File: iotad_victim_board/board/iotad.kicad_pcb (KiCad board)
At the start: 2 copper layers, 24.8 x 29 mm, 5 parts, among them P1 CONN_01X09, P2 CONN_01X06, U1 24C16, U2 MAX31820

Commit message: today
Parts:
- removed the P1 at (125.9, 124.6)
- removed the P2 at (143.9, 111.0)
- removed the R1 at (131.4, 124.7)
- removed the U1 at (134.4, 112.6)
- removed the U2 at (141.3, 123.8)
- added P1: CONN_01X09, Pin_Headers:Pin_Header_Straight_1x09, F.Cu at (153.4, 124.2)
- added P1: CONN_01X09, Pin_Headers:Pin_Header_Straight_1x09, F.Cu at (139.4, 124.2)
- added P2: CONN_01X06, Pin_Headers:Pin_Header_Straight_1x06, F.Cu at (163.1, 103.9)
- added P2: CONN_01X06, Pin_Headers:Pin_Header_Straight_1x06, F.Cu at (149.1, 103.9)
- added R1: 4.8k, Resistors_SMD:R_1206_HandSoldering, F.Cu at (158.2, 115.6)
- added R1: 4.8k, Resistors_SMD:R_1206_HandSoldering, F.Cu at (144.3, 115.6)
- added REF**11111: via, via, F.Cu at (152.7, 127.5)
- added REF**11111: via, via, F.Cu at (160.3, 126.2)
- added REF**11111: via, via, F.Cu at (160.5, 119.1)
- added REF**11111: via, via, F.Cu at (156.7, 106.4)
- added REF**11111: via, via, F.Cu at (146.3, 126.2)
- added REF**11111: via, via, F.Cu at (138.7, 127.5)
- added REF**11111: via, via, F.Cu at (146.6, 119.1)
- added REF**11111: via, via, F.Cu at (142.7, 106.4)
- added REF**11121: via, via, F.Cu at (161.8, 126.2)
- added REF**11121: via, via, F.Cu at (154.2, 127.5)
- added REF**11121: via, via, F.Cu at (162.0, 119.1)
- added REF**11121: via, via, F.Cu at (158.2, 106.4)
- added REF**11121: via, via, F.Cu at (147.8, 126.2)
- added REF**11121: via, via, F.Cu at (140.2, 127.5)
- added REF**11121: via, via, F.Cu at (148.1, 119.1)
- added REF**11121: via, via, F.Cu at (144.2, 106.4)
- added REF**11131: via, via, F.Cu at (155.7, 127.5)
- added REF**11131: via, via, F.Cu at (163.5, 119.1)
- added REF**11131: via, via, F.Cu at (163.3, 126.2)
- added REF**11131: via, via, F.Cu at (159.7, 106.4)
- added REF**11131: via, via, F.Cu at (149.3, 126.2)
- added REF**11131: via, via, F.Cu at (141.7, 127.5)
- added REF**11131: via, via, F.Cu at (149.6, 119.1)
- added REF**11131: via, via, F.Cu at (145.7, 106.4)
- added U1: 24C16, SMD_Packages:SOIC-8-N, F.Cu at (158.5, 106.2)
- added U1: 24C16, SMD_Packages:SOIC-8-N, F.Cu at (144.5, 106.2)
- added U2: MAX31820, TO_SOT_Packages_THT:TO-92_Molded_Wide, F.Cu at (163.6, 121.9)
- added U2: MAX31820, TO_SOT_Packages_THT:TO-92_Molded_Wide, F.Cu at (149.6, 121.9)
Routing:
- net VCC: track 45.2 -> 61.2 mm
- net DATA: track 13.7 -> 29.5 mm
- net TX: track 18.3 -> 28.3 mm
- net RX: track 18.3 -> 26.5 mm
- net SCL: track 5.30 -> 11.6 mm
- net SDA: track 5.82 -> 6.67 mm
- added copper zone on B.Cu, net Net-(P1-Pad8)
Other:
- board size 24.8 x 29 mm -> 27.9 x 27.9 mm
- board text added: "3.3v"
- board text added: "D1W"
- board text added: "GND"
- board text added: "IoTAD Victim Board v1.01"
- board text added: "RX"
- board text added: "SCL"
- board text added: "SDA"
- board text added: "TX"
- board text added: "dsgn: jegeva 2016"

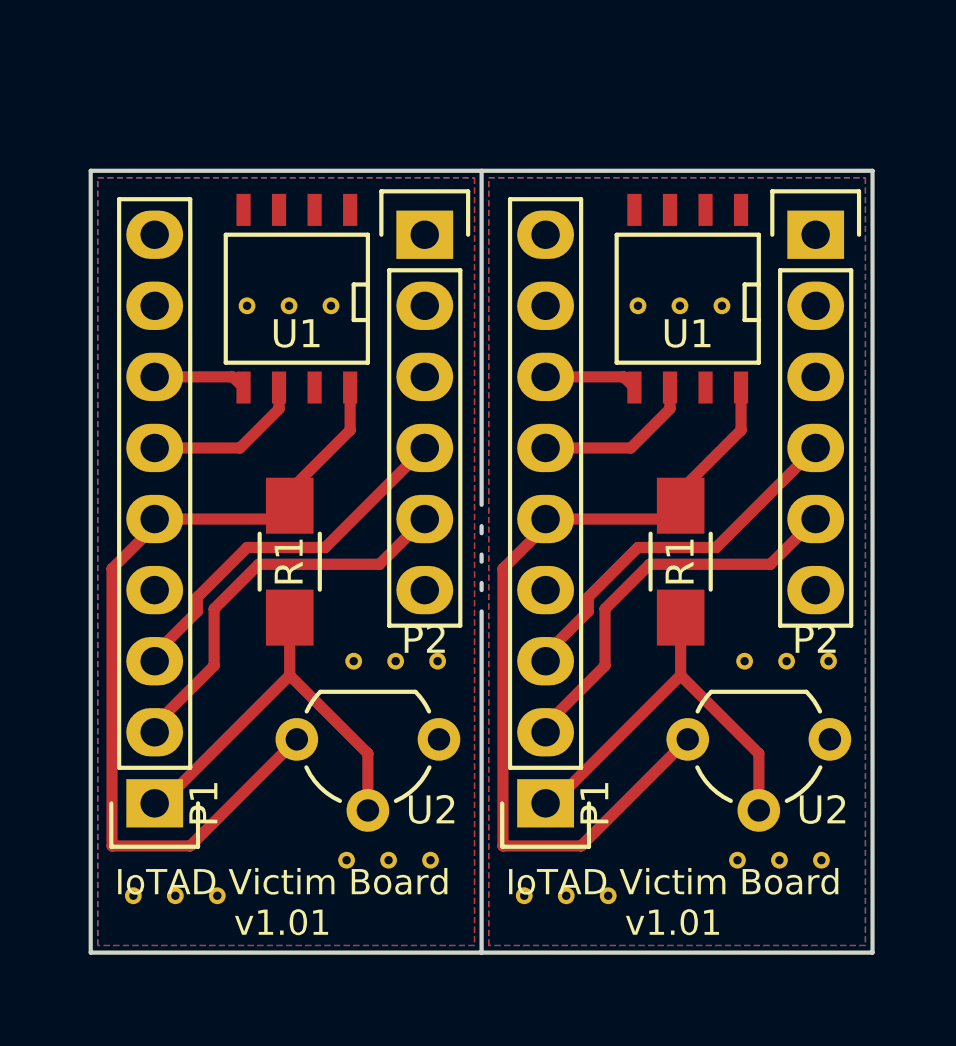
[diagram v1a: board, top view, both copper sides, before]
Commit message: harcoded password
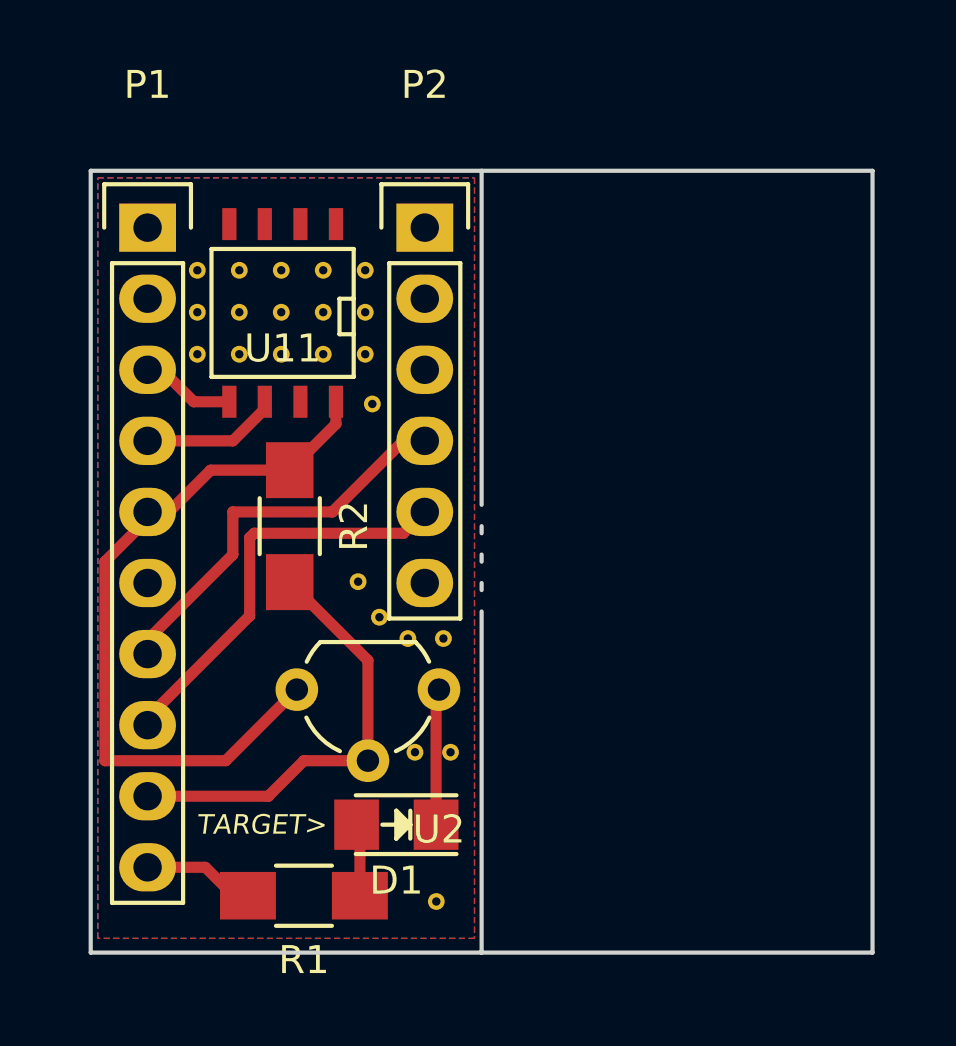
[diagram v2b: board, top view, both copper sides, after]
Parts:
- removed the P1 at (153.4, 124.2)
- removed the P1 at (139.4, 124.2)
- removed the P2 at (163.1, 103.9)
- removed the P2 at (149.1, 103.9)
- removed the R1 at (158.2, 115.6)
- removed the R1 at (144.3, 115.6)
- removed REF**11111 (x8), REF**11121 (x8), REF**11131 (x8): via, via
- removed U1 (x2): 24C16, SMD_Packages:SOIC-8-N
- removed the U2 at (163.6, 121.9)
- removed the U2 at (149.6, 121.9)
- added D1: LED, LEDs:LED_1206, F.Cu at (148.1, 125.0)
- added P1: CONN_01X10, Pin_Headers:Pin_Header_Straight_1x10, F.Cu at (139.2, 103.6)
- added P2: CONN_01X06, Pin_Headers:Pin_Header_Straight_1x06, F.Cu at (149.1, 103.6)
- added R1: R, Resistors_SMD:R_1206_HandSoldering, F.Cu at (144.8, 127.5)
- added R2: 4.8k, Resistors_SMD:R_1206_HandSoldering, F.Cu at (144.3, 114.3)
- added REF**1111: VIA-0.6mm, via-0:VIA-0.6mm, F.Cu at (141.0, 105.2)
- added REF**1112: VIA-0.6mm, via-0:VIA-0.6mm, F.Cu at (141.0, 106.7)
- added REF**1113: VIA-0.6mm, via-0:VIA-0.6mm, F.Cu at (141.0, 108.2)
- added REF**1121: VIA-0.6mm, via-0:VIA-0.6mm, F.Cu at (142.5, 105.2)
- added REF**1122: VIA-0.6mm, via-0:VIA-0.6mm, F.Cu at (142.5, 106.7)
- added REF**1123: VIA-0.6mm, via-0:VIA-0.6mm, F.Cu at (142.5, 108.2)
- added REF**1131: VIA-0.6mm, via-0:VIA-0.6mm, F.Cu at (144.0, 105.2)
- added REF**1132: VIA-0.6mm, via-0:VIA-0.6mm, F.Cu at (144.0, 106.7)
- added REF**1133: VIA-0.6mm, via-0:VIA-0.6mm, F.Cu at (144.0, 108.2)
- added REF**1141: VIA-0.6mm, via-0:VIA-0.6mm, F.Cu at (145.5, 105.2)
- added REF**1142: VIA-0.6mm, via-0:VIA-0.6mm, F.Cu at (145.5, 106.7)
- added REF**1143: VIA-0.6mm, via-0:VIA-0.6mm, F.Cu at (145.5, 108.2)
- added REF**1151: VIA-0.6mm, via-0:VIA-0.6mm, F.Cu at (147.0, 105.2)
- added REF**1152: VIA-0.6mm, via-0:VIA-0.6mm, F.Cu at (147.0, 106.7)
- added REF**1153: VIA-0.6mm, via-0:VIA-0.6mm, F.Cu at (149.5, 127.7)
- added REF**1153: VIA-0.6mm, via-0:VIA-0.6mm, F.Cu at (148.7, 122.4)
- added REF**1153: VIA-0.6mm, via-0:VIA-0.6mm, F.Cu at (150.0, 122.4)
- added REF**1153: VIA-0.6mm, via-0:VIA-0.6mm, F.Cu at (148.5, 118.3)
- added REF**1153: VIA-0.6mm, via-0:VIA-0.6mm, F.Cu at (149.8, 118.3)
- added REF**1153: VIA-0.6mm, via-0:VIA-0.6mm, F.Cu at (147.5, 117.6)
- added REF**1153: VIA-0.6mm, via-0:VIA-0.6mm, F.Cu at (146.7, 116.3)
- added REF**1153: VIA-0.6mm, via-0:VIA-0.6mm, F.Cu at (147.2, 109.9)
- added REF**1153: VIA-0.6mm, via-0:VIA-0.6mm, F.Cu at (147.0, 108.2)
- added U11: 24C16, SMD_Packages:SOIC-8-N, F.Cu at (144.0, 106.7)
- added U2: MAX31820, TO_SOT_Packages_THT:TO-92_Molded_Wide, F.Cu at (149.6, 120.1)
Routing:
- net VCC: track 61.2 -> 26.3 mm
- net DATA: track 29.5 -> 15.9 mm
- net TX: track 28.3 -> 14.8 mm
- net RX: track 26.5 -> 14.3 mm
- net SCL: track 11.6 -> 4.92 mm
- net GND: track 0.00 -> 4.87 mm
- net Net-(P1-Pad10): track 0.00 -> 4.22 mm
- net SDA: track 6.67 -> 3.39 mm
- net Net-(D1-Pad2): track 0.00 -> 2.59 mm
- added copper zone on B.Cu, net GND
- added copper zone on F.Cu, net GND
- removed copper zone on B.Cu, net Net-(P1-Pad8)
- removed copper zone on F.Cu, net Net-(P1-Pad8)
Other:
- board text added: "IoTAD v1.2 24/02/2016 JGV"
- board text added: "Rx"
- board text added: "TARGET>"
- board text added: "Tx"
- board text added: "T° Data"
- board text added: "VCC"
- board text removed: "3.3v"
- board text removed: "D1W"
- board text removed: "IoTAD Victim Board v1.01"
- board text removed: "RX"
- board text removed: "TX"
- board text removed: "dsgn: jegeva 2016"

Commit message: storing
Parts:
- added D1: LED, LEDs:LED_1206, F.Cu at (182.6, 127.5)
- added D1: LED, LEDs:LED_1206, F.Cu at (197.4, 127.5)
- added D1: LED, LEDs:LED_1206, F.Cu at (227.1, 127.5)
- added D1: LED, LEDs:LED_1206, F.Cu at (212.3, 127.5)
- added D1: LED, LEDs:LED_1206, F.Cu at (153.2, 127.5)
- added D1: LED, LEDs:LED_1206, F.Cu at (167.9, 127.5)
- added D1: LED, LEDs:LED_1206, F.Cu at (138.2, 127.5)
- added P1: CONN_01X10, Pin_Headers:Pin_Header_Straight_1x10, F.Cu at (173.7, 106.2)
- added P1: CONN_01X10, Pin_Headers:Pin_Header_Straight_1x10, F.Cu at (188.5, 106.2)
- added P1: CONN_01X10, Pin_Headers:Pin_Header_Straight_1x10, F.Cu at (218.2, 106.2)
- added P1: CONN_01X10, Pin_Headers:Pin_Header_Straight_1x10, F.Cu at (203.5, 106.2)
- added P1: CONN_01X10, Pin_Headers:Pin_Header_Straight_1x10, F.Cu at (144.3, 106.2)
- added P1: CONN_01X10, Pin_Headers:Pin_Header_Straight_1x10, F.Cu at (159.0, 106.2)
- added P1: CONN_01X10, Pin_Headers:Pin_Header_Straight_1x10, F.Cu at (129.3, 106.2)
- added P2: CONN_01X06, Pin_Headers:Pin_Header_Straight_1x06, F.Cu at (183.6, 118.4)
- added P2: CONN_01X06, Pin_Headers:Pin_Header_Straight_1x06, F.Cu at (198.4, 118.4)
- added P2: CONN_01X06, Pin_Headers:Pin_Header_Straight_1x06, F.Cu at (228.1, 118.4)
- added P2: CONN_01X06, Pin_Headers:Pin_Header_Straight_1x06, F.Cu at (213.4, 118.4)
- added P2: CONN_01X06, Pin_Headers:Pin_Header_Straight_1x06, F.Cu at (154.2, 118.4)
- added P2: CONN_01X06, Pin_Headers:Pin_Header_Straight_1x06, F.Cu at (168.9, 118.4)
- added P2: CONN_01X06, Pin_Headers:Pin_Header_Straight_1x06, F.Cu at (139.2, 118.4)
- added R1: R, Resistors_SMD:R_1206_HandSoldering, F.Cu at (179.3, 130.0)
- added R1: R, Resistors_SMD:R_1206_HandSoldering, F.Cu at (194.1, 130.0)
- added R1: R, Resistors_SMD:R_1206_HandSoldering, F.Cu at (223.8, 130.0)
- added R1: R, Resistors_SMD:R_1206_HandSoldering, F.Cu at (209.0, 130.0)
- added R1: R, Resistors_SMD:R_1206_HandSoldering, F.Cu at (149.9, 130.0)
- added R1: R, Resistors_SMD:R_1206_HandSoldering, F.Cu at (164.6, 130.0)
- added R1: R, Resistors_SMD:R_1206_HandSoldering, F.Cu at (134.9, 130.0)
- added R2: 4.8k, Resistors_SMD:R_1206_HandSoldering, F.Cu at (178.8, 116.8)
- added R2: 4.8k, Resistors_SMD:R_1206_HandSoldering, F.Cu at (193.5, 116.8)
- added R2: 4.8k, Resistors_SMD:R_1206_HandSoldering, F.Cu at (223.3, 116.8)
- added R2: 4.8k, Resistors_SMD:R_1206_HandSoldering, F.Cu at (208.5, 116.8)
- added R2: 4.8k, Resistors_SMD:R_1206_HandSoldering, F.Cu at (149.4, 116.8)
- added R2: 4.8k, Resistors_SMD:R_1206_HandSoldering, F.Cu at (164.1, 116.8)
- added R2: 4.8k, Resistors_SMD:R_1206_HandSoldering, F.Cu at (134.4, 116.8)
- added REF** (x4): DRILL-0.6mm, via-0:DRILL-0.6mm, F.Cu at (186.2, 107.7)
- added REF** (x4): DRILL-0.6mm, via-0:DRILL-0.6mm, F.Cu at (186.2, 104.6)
- added REF** (x4): DRILL-0.6mm, via-0:DRILL-0.6mm, F.Cu at (186.2, 121.9)
- added REF** (x4): DRILL-0.6mm, via-0:DRILL-0.6mm, F.Cu at (186.2, 124.0)
- added REF** (x4): DRILL-0.6mm, via-0:DRILL-0.6mm, F.Cu at (186.2, 122.9)
- added REF** (x4): DRILL-0.6mm, via-0:DRILL-0.6mm, F.Cu at (215.9, 124.0)
- added REF** (x4): DRILL-0.6mm, via-0:DRILL-0.6mm, F.Cu at (215.9, 122.9)
- added REF** (x4): DRILL-0.6mm, via-0:DRILL-0.6mm, F.Cu at (215.9, 121.9)
- added REF** (x4): DRILL-0.6mm, via-0:DRILL-0.6mm, F.Cu at (215.9, 120.9)
- added REF** (x4): DRILL-0.6mm, via-0:DRILL-0.6mm, F.Cu at (186.2, 105.7)
- added REF** (x4): DRILL-0.6mm, via-0:DRILL-0.6mm, F.Cu at (215.9, 126.0)
- added REF** (x4): DRILL-0.6mm, via-0:DRILL-0.6mm, F.Cu at (215.9, 125.0)
- added REF** (x4): DRILL-0.6mm, via-0:DRILL-0.6mm, F.Cu at (215.9, 128.0)
- added REF** (x4): DRILL-0.6mm, via-0:DRILL-0.6mm, F.Cu at (215.9, 127.0)
- added REF** (x4): DRILL-0.6mm, via-0:DRILL-0.6mm, F.Cu at (215.9, 130.0)
- added REF** (x4): DRILL-0.6mm, via-0:DRILL-0.6mm, F.Cu at (215.9, 129.0)
- added REF** (x4): DRILL-0.6mm, via-0:DRILL-0.6mm, F.Cu at (215.9, 131.1)
- added REF** (x4): DRILL-0.6mm, via-0:DRILL-0.6mm, F.Cu at (215.9, 115.8)
- added REF** (x4): DRILL-0.6mm, via-0:DRILL-0.6mm, F.Cu at (215.9, 114.8)
- added REF** (x4): DRILL-0.6mm, via-0:DRILL-0.6mm, F.Cu at (215.9, 113.8)
- added REF** (x4): DRILL-0.6mm, via-0:DRILL-0.6mm, F.Cu at (215.9, 112.8)
- added REF** (x4): DRILL-0.6mm, via-0:DRILL-0.6mm, F.Cu at (215.9, 117.9)
- added REF** (x4): DRILL-0.6mm, via-0:DRILL-0.6mm, F.Cu at (186.2, 109.7)
- added REF** (x4): DRILL-0.6mm, via-0:DRILL-0.6mm, F.Cu at (215.9, 116.8)
- added REF** (x4): DRILL-0.6mm, via-0:DRILL-0.6mm, F.Cu at (215.9, 119.9)
- added REF** (x4): DRILL-0.6mm, via-0:DRILL-0.6mm, F.Cu at (215.9, 118.9)
- added REF** (x4): DRILL-0.6mm, via-0:DRILL-0.6mm, F.Cu at (186.2, 108.7)
- added REF** (x4): DRILL-0.6mm, via-0:DRILL-0.6mm, F.Cu at (215.9, 111.8)
- added REF** (x4): DRILL-0.6mm, via-0:DRILL-0.6mm, F.Cu at (215.9, 110.7)
- added REF** (x4): DRILL-0.6mm, via-0:DRILL-0.6mm, F.Cu at (215.9, 109.7)
- added REF** (x4): DRILL-0.6mm, via-0:DRILL-0.6mm, F.Cu at (215.9, 108.7)
- added REF** (x4): DRILL-0.6mm, via-0:DRILL-0.6mm, F.Cu at (186.2, 106.7)
- added REF** (x4): DRILL-0.6mm, via-0:DRILL-0.6mm, F.Cu at (215.9, 105.7)
- added REF** (x4): DRILL-0.6mm, via-0:DRILL-0.6mm, F.Cu at (215.9, 104.6)
- added REF** (x4): DRILL-0.6mm, via-0:DRILL-0.6mm, F.Cu at (215.9, 107.7)
- added REF** (x4): DRILL-0.6mm, via-0:DRILL-0.6mm, F.Cu at (215.9, 106.7)
- added REF** (x4): DRILL-0.6mm, via-0:DRILL-0.6mm, F.Cu at (200.9, 124.2)
- added REF** (x4): DRILL-0.6mm, via-0:DRILL-0.6mm, F.Cu at (200.9, 123.2)
- added REF** (x4): DRILL-0.6mm, via-0:DRILL-0.6mm, F.Cu at (200.9, 122.2)
- added REF** (x4): DRILL-0.6mm, via-0:DRILL-0.6mm, F.Cu at (200.9, 121.2)
- added REF** (x4): DRILL-0.6mm, via-0:DRILL-0.6mm, F.Cu at (200.9, 126.2)
- added REF** (x4): DRILL-0.6mm, via-0:DRILL-0.6mm, F.Cu at (200.9, 125.2)
- added REF** (x4): DRILL-0.6mm, via-0:DRILL-0.6mm, F.Cu at (200.9, 128.3)
- added REF** (x4): DRILL-0.6mm, via-0:DRILL-0.6mm, F.Cu at (200.9, 127.3)
- added REF** (x4): DRILL-0.6mm, via-0:DRILL-0.6mm, F.Cu at (200.9, 130.3)
- added REF** (x4): DRILL-0.6mm, via-0:DRILL-0.6mm, F.Cu at (186.2, 111.8)
- added REF** (x4): DRILL-0.6mm, via-0:DRILL-0.6mm, F.Cu at (200.9, 129.3)
- added REF** (x4): DRILL-0.6mm, via-0:DRILL-0.6mm, F.Cu at (200.9, 131.3)
- added REF** (x4): DRILL-0.6mm, via-0:DRILL-0.6mm, F.Cu at (186.2, 110.7)
- added REF** (x4): DRILL-0.6mm, via-0:DRILL-0.6mm, F.Cu at (200.9, 116.1)
- added REF** (x4): DRILL-0.6mm, via-0:DRILL-0.6mm, F.Cu at (200.9, 115.1)
- added REF** (x4): DRILL-0.6mm, via-0:DRILL-0.6mm, F.Cu at (200.9, 114.0)
- added REF** (x4): DRILL-0.6mm, via-0:DRILL-0.6mm, F.Cu at (200.9, 113.0)
- added REF** (x4): DRILL-0.6mm, via-0:DRILL-0.6mm, F.Cu at (200.9, 118.1)
- added REF** (x4): DRILL-0.6mm, via-0:DRILL-0.6mm, F.Cu at (200.9, 117.1)
- added REF** (x4): DRILL-0.6mm, via-0:DRILL-0.6mm, F.Cu at (200.9, 120.1)
- added REF** (x4): DRILL-0.6mm, via-0:DRILL-0.6mm, F.Cu at (200.9, 119.1)
- added REF** (x4): DRILL-0.6mm, via-0:DRILL-0.6mm, F.Cu at (200.9, 112.0)
- added REF** (x4): DRILL-0.6mm, via-0:DRILL-0.6mm, F.Cu at (200.9, 111.0)
- added REF** (x4): DRILL-0.6mm, via-0:DRILL-0.6mm, F.Cu at (200.9, 110.0)
- added REF** (x4): DRILL-0.6mm, via-0:DRILL-0.6mm, F.Cu at (200.9, 109.0)
- added REF** (x4): DRILL-0.6mm, via-0:DRILL-0.6mm, F.Cu at (200.9, 105.9)
- added REF** (x4): DRILL-0.6mm, via-0:DRILL-0.6mm, F.Cu at (200.9, 104.9)
- added REF** (x4): DRILL-0.6mm, via-0:DRILL-0.6mm, F.Cu at (200.9, 108.0)
- added REF** (x4): DRILL-0.6mm, via-0:DRILL-0.6mm, F.Cu at (200.9, 106.9)
- added REF** (x4): DRILL-0.6mm, via-0:DRILL-0.6mm, F.Cu at (141.7, 108.0)
- added REF** (x4): DRILL-0.6mm, via-0:DRILL-0.6mm, F.Cu at (141.7, 106.9)
- added REF** (x4): DRILL-0.6mm, via-0:DRILL-0.6mm, F.Cu at (186.2, 119.9)
- added REF** (x4): DRILL-0.6mm, via-0:DRILL-0.6mm, F.Cu at (141.7, 105.9)
- added REF** (x4): DRILL-0.6mm, via-0:DRILL-0.6mm, F.Cu at (141.7, 104.9)
- added REF** (x4): DRILL-0.6mm, via-0:DRILL-0.6mm, F.Cu at (186.2, 118.9)
- added REF** (x4): DRILL-0.6mm, via-0:DRILL-0.6mm, F.Cu at (141.7, 110.0)
- added REF** (x4): DRILL-0.6mm, via-0:DRILL-0.6mm, F.Cu at (141.7, 109.0)
- added REF** (x4): DRILL-0.6mm, via-0:DRILL-0.6mm, F.Cu at (141.7, 112.0)
- added REF** (x4): DRILL-0.6mm, via-0:DRILL-0.6mm, F.Cu at (141.7, 111.0)
- added REF** (x4): DRILL-0.6mm, via-0:DRILL-0.6mm, F.Cu at (141.7, 120.1)
- added REF** (x4): DRILL-0.6mm, via-0:DRILL-0.6mm, F.Cu at (141.7, 119.1)
- added REF** (x4): DRILL-0.6mm, via-0:DRILL-0.6mm, F.Cu at (141.7, 118.1)
- added REF** (x4): DRILL-0.6mm, via-0:DRILL-0.6mm, F.Cu at (141.7, 117.1)
- added REF** (x4): DRILL-0.6mm, via-0:DRILL-0.6mm, F.Cu at (141.7, 114.0)
- added REF** (x4): DRILL-0.6mm, via-0:DRILL-0.6mm, F.Cu at (141.7, 113.0)
- added REF** (x4): DRILL-0.6mm, via-0:DRILL-0.6mm, F.Cu at (141.7, 116.1)
- added REF** (x4): DRILL-0.6mm, via-0:DRILL-0.6mm, F.Cu at (141.7, 115.1)
- added REF** (x4): DRILL-0.6mm, via-0:DRILL-0.6mm, F.Cu at (141.7, 131.3)
- added REF** (x4): DRILL-0.6mm, via-0:DRILL-0.6mm, F.Cu at (141.7, 130.3)
- added REF** (x4): DRILL-0.6mm, via-0:DRILL-0.6mm, F.Cu at (141.7, 129.3)
- added REF** (x4): DRILL-0.6mm, via-0:DRILL-0.6mm, F.Cu at (141.7, 128.3)
- added REF** (x4): DRILL-0.6mm, via-0:DRILL-0.6mm, F.Cu at (141.7, 127.3)
- added REF** (x4): DRILL-0.6mm, via-0:DRILL-0.6mm, F.Cu at (141.7, 126.2)
- added REF** (x4): DRILL-0.6mm, via-0:DRILL-0.6mm, F.Cu at (186.2, 117.9)
- added REF** (x4): DRILL-0.6mm, via-0:DRILL-0.6mm, F.Cu at (141.7, 125.2)
- added REF** (x4): DRILL-0.6mm, via-0:DRILL-0.6mm, F.Cu at (141.7, 122.2)
- added REF** (x4): DRILL-0.6mm, via-0:DRILL-0.6mm, F.Cu at (141.7, 121.2)
- added REF** (x4): DRILL-0.6mm, via-0:DRILL-0.6mm, F.Cu at (186.2, 116.8)
- added REF** (x4): DRILL-0.6mm, via-0:DRILL-0.6mm, F.Cu at (141.7, 124.2)
- added REF** (x4): DRILL-0.6mm, via-0:DRILL-0.6mm, F.Cu at (141.7, 123.2)
- added REF** (x4): DRILL-0.6mm, via-0:DRILL-0.6mm, F.Cu at (171.4, 124.0)
- added REF** (x4): DRILL-0.6mm, via-0:DRILL-0.6mm, F.Cu at (171.4, 122.9)
- added REF** (x4): DRILL-0.6mm, via-0:DRILL-0.6mm, F.Cu at (171.4, 121.9)
- added REF** (x4): DRILL-0.6mm, via-0:DRILL-0.6mm, F.Cu at (171.4, 120.9)
- added REF** (x4): DRILL-0.6mm, via-0:DRILL-0.6mm, F.Cu at (171.4, 126.0)
- added REF** (x4): DRILL-0.6mm, via-0:DRILL-0.6mm, F.Cu at (171.4, 125.0)
- added REF** (x4): DRILL-0.6mm, via-0:DRILL-0.6mm, F.Cu at (171.4, 128.0)
- added REF** (x4): DRILL-0.6mm, via-0:DRILL-0.6mm, F.Cu at (171.4, 127.0)
- added REF** (x4): DRILL-0.6mm, via-0:DRILL-0.6mm, F.Cu at (171.4, 130.0)
- added REF** (x4): DRILL-0.6mm, via-0:DRILL-0.6mm, F.Cu at (171.4, 129.0)
- added REF** (x4): DRILL-0.6mm, via-0:DRILL-0.6mm, F.Cu at (171.4, 131.1)
- added REF** (x4): DRILL-0.6mm, via-0:DRILL-0.6mm, F.Cu at (171.4, 115.8)
- added REF** (x4): DRILL-0.6mm, via-0:DRILL-0.6mm, F.Cu at (171.4, 114.8)
- added REF** (x4): DRILL-0.6mm, via-0:DRILL-0.6mm, F.Cu at (171.4, 113.8)
- added REF** (x4): DRILL-0.6mm, via-0:DRILL-0.6mm, F.Cu at (171.4, 112.8)
- added REF** (x4): DRILL-0.6mm, via-0:DRILL-0.6mm, F.Cu at (186.2, 113.8)
- added REF** (x4): DRILL-0.6mm, via-0:DRILL-0.6mm, F.Cu at (171.4, 117.9)
- added REF** (x4): DRILL-0.6mm, via-0:DRILL-0.6mm, F.Cu at (171.4, 116.8)
- added REF** (x4): DRILL-0.6mm, via-0:DRILL-0.6mm, F.Cu at (186.2, 112.8)
- added REF** (x4): DRILL-0.6mm, via-0:DRILL-0.6mm, F.Cu at (171.4, 119.9)
- added REF** (x4): DRILL-0.6mm, via-0:DRILL-0.6mm, F.Cu at (171.4, 118.9)
- added REF** (x4): DRILL-0.6mm, via-0:DRILL-0.6mm, F.Cu at (171.4, 111.8)
- added REF** (x4): DRILL-0.6mm, via-0:DRILL-0.6mm, F.Cu at (171.4, 110.7)
- added REF** (x4): DRILL-0.6mm, via-0:DRILL-0.6mm, F.Cu at (171.4, 109.7)
- added REF** (x4): DRILL-0.6mm, via-0:DRILL-0.6mm, F.Cu at (171.4, 108.7)
- added REF** (x4): DRILL-0.6mm, via-0:DRILL-0.6mm, F.Cu at (171.4, 105.7)
- added REF** (x4): DRILL-0.6mm, via-0:DRILL-0.6mm, F.Cu at (171.4, 104.6)
- added REF** (x4): DRILL-0.6mm, via-0:DRILL-0.6mm, F.Cu at (171.4, 107.7)
- added REF** (x4): DRILL-0.6mm, via-0:DRILL-0.6mm, F.Cu at (171.4, 106.7)
- added REF** (x4): DRILL-0.6mm, via-0:DRILL-0.6mm, F.Cu at (156.7, 107.7)
- added REF** (x4): DRILL-0.6mm, via-0:DRILL-0.6mm, F.Cu at (156.7, 106.7)
- added REF** (x4): DRILL-0.6mm, via-0:DRILL-0.6mm, F.Cu at (156.7, 105.7)
- added REF** (x4): DRILL-0.6mm, via-0:DRILL-0.6mm, F.Cu at (156.7, 104.6)
- added REF** (x4): DRILL-0.6mm, via-0:DRILL-0.6mm, F.Cu at (156.7, 109.7)
- added REF** (x4): DRILL-0.6mm, via-0:DRILL-0.6mm, F.Cu at (156.7, 108.7)
- added REF** (x4): DRILL-0.6mm, via-0:DRILL-0.6mm, F.Cu at (156.7, 111.8)
- added REF** (x4): DRILL-0.6mm, via-0:DRILL-0.6mm, F.Cu at (156.7, 110.7)
- added REF** (x4): DRILL-0.6mm, via-0:DRILL-0.6mm, F.Cu at (186.2, 115.8)
- added REF** (x4): DRILL-0.6mm, via-0:DRILL-0.6mm, F.Cu at (156.7, 119.9)
- added REF** (x4): DRILL-0.6mm, via-0:DRILL-0.6mm, F.Cu at (156.7, 118.9)
- added REF** (x4): DRILL-0.6mm, via-0:DRILL-0.6mm, F.Cu at (186.2, 114.8)
- added REF** (x4): DRILL-0.6mm, via-0:DRILL-0.6mm, F.Cu at (156.7, 117.9)
- added REF** (x4): DRILL-0.6mm, via-0:DRILL-0.6mm, F.Cu at (156.7, 116.8)
- added REF** (x4): DRILL-0.6mm, via-0:DRILL-0.6mm, F.Cu at (156.7, 113.8)
- added REF** (x4): DRILL-0.6mm, via-0:DRILL-0.6mm, F.Cu at (156.7, 112.8)
- added REF** (x4): DRILL-0.6mm, via-0:DRILL-0.6mm, F.Cu at (156.7, 115.8)
- added REF** (x4): DRILL-0.6mm, via-0:DRILL-0.6mm, F.Cu at (156.7, 114.8)
- added REF** (x4): DRILL-0.6mm, via-0:DRILL-0.6mm, F.Cu at (156.7, 131.1)
- added REF** (x4): DRILL-0.6mm, via-0:DRILL-0.6mm, F.Cu at (156.7, 130.0)
- added REF** (x4): DRILL-0.6mm, via-0:DRILL-0.6mm, F.Cu at (156.7, 129.0)
- added REF** (x4): DRILL-0.6mm, via-0:DRILL-0.6mm, F.Cu at (156.7, 128.0)
- added REF** (x4): DRILL-0.6mm, via-0:DRILL-0.6mm, F.Cu at (156.7, 127.0)
- added REF** (x4): DRILL-0.6mm, via-0:DRILL-0.6mm, F.Cu at (156.7, 126.0)
- added REF** (x4): DRILL-0.6mm, via-0:DRILL-0.6mm, F.Cu at (156.7, 125.0)
- added REF** (x4): DRILL-0.6mm, via-0:DRILL-0.6mm, F.Cu at (156.7, 121.9)
- added REF** (x4): DRILL-0.6mm, via-0:DRILL-0.6mm, F.Cu at (156.7, 120.9)
- added REF** (x4): DRILL-0.6mm, via-0:DRILL-0.6mm, F.Cu at (156.7, 124.0)
- added REF** (x4): DRILL-0.6mm, via-0:DRILL-0.6mm, F.Cu at (156.7, 122.9)
- added REF** (x4): DRILL-0.6mm, via-0:DRILL-0.6mm, F.Cu at (127.0, 124.0)
- added REF** (x4): DRILL-0.6mm, via-0:DRILL-0.6mm, F.Cu at (186.2, 131.1)
- added REF** (x4): DRILL-0.6mm, via-0:DRILL-0.6mm, F.Cu at (127.0, 122.9)
- added REF** (x4): DRILL-0.6mm, via-0:DRILL-0.6mm, F.Cu at (127.0, 121.9)
- added REF** (x4): DRILL-0.6mm, via-0:DRILL-0.6mm, F.Cu at (127.0, 120.9)
- added REF** (x4): DRILL-0.6mm, via-0:DRILL-0.6mm, F.Cu at (127.0, 126.0)
- added REF** (x4): DRILL-0.6mm, via-0:DRILL-0.6mm, F.Cu at (127.0, 125.0)
- added REF** (x4): DRILL-0.6mm, via-0:DRILL-0.6mm, F.Cu at (127.0, 128.0)
- added REF** (x4): DRILL-0.6mm, via-0:DRILL-0.6mm, F.Cu at (127.0, 127.0)
- added REF** (x4): DRILL-0.6mm, via-0:DRILL-0.6mm, F.Cu at (127.0, 130.0)
- added REF** (x4): DRILL-0.6mm, via-0:DRILL-0.6mm, F.Cu at (127.0, 129.0)
- added REF** (x4): DRILL-0.6mm, via-0:DRILL-0.6mm, F.Cu at (127.0, 131.1)
- added REF** (x4): DRILL-0.6mm, via-0:DRILL-0.6mm, F.Cu at (186.2, 130.0)
- added REF** (x4): DRILL-0.6mm, via-0:DRILL-0.6mm, F.Cu at (127.0, 115.8)
- added REF** (x4): DRILL-0.6mm, via-0:DRILL-0.6mm, F.Cu at (127.0, 114.8)
- added REF** (x4): DRILL-0.6mm, via-0:DRILL-0.6mm, F.Cu at (186.2, 129.0)
- added REF** (x4): DRILL-0.6mm, via-0:DRILL-0.6mm, F.Cu at (127.0, 113.8)
- added REF** (x4): DRILL-0.6mm, via-0:DRILL-0.6mm, F.Cu at (127.0, 112.8)
- added REF** (x4): DRILL-0.6mm, via-0:DRILL-0.6mm, F.Cu at (127.0, 117.9)
- added REF** (x4): DRILL-0.6mm, via-0:DRILL-0.6mm, F.Cu at (127.0, 116.8)
- added REF** (x4): DRILL-0.6mm, via-0:DRILL-0.6mm, F.Cu at (127.0, 119.9)
- added REF** (x4): DRILL-0.6mm, via-0:DRILL-0.6mm, F.Cu at (127.0, 118.9)
- added REF** (x4): DRILL-0.6mm, via-0:DRILL-0.6mm, F.Cu at (127.0, 111.8)
- added REF** (x4): DRILL-0.6mm, via-0:DRILL-0.6mm, F.Cu at (127.0, 110.7)
- added REF** (x4): DRILL-0.6mm, via-0:DRILL-0.6mm, F.Cu at (127.0, 109.7)
- added REF** (x4): DRILL-0.6mm, via-0:DRILL-0.6mm, F.Cu at (127.0, 108.7)
- added REF** (x4): DRILL-0.6mm, via-0:DRILL-0.6mm, F.Cu at (127.0, 105.7)
- added REF** (x4): DRILL-0.6mm, via-0:DRILL-0.6mm, F.Cu at (127.0, 104.6)
- added REF** (x4): DRILL-0.6mm, via-0:DRILL-0.6mm, F.Cu at (127.0, 107.7)
- added REF** (x4): DRILL-0.6mm, via-0:DRILL-0.6mm, F.Cu at (127.0, 106.7)
- added REF** (x4): DRILL-0.6mm, via-0:DRILL-0.6mm, F.Cu at (186.2, 128.0)
- added REF** (x4): DRILL-0.6mm, via-0:DRILL-0.6mm, F.Cu at (186.2, 127.0)
- added REF** (x4): DRILL-0.6mm, via-0:DRILL-0.6mm, F.Cu at (186.2, 126.0)
- added REF** (x4): DRILL-0.6mm, via-0:DRILL-0.6mm, F.Cu at (186.2, 125.0)
- added REF** (x4): DRILL-0.6mm, via-0:DRILL-0.6mm, F.Cu at (186.2, 120.9)
- added REF**1111: VIA-0.6mm, via-0:VIA-0.6mm, F.Cu at (175.5, 107.7)
- added REF**1111: VIA-0.6mm, via-0:VIA-0.6mm, F.Cu at (190.2, 107.7)
- added REF**1111: VIA-0.6mm, via-0:VIA-0.6mm, F.Cu at (220.0, 107.7)
- added REF**1111: VIA-0.6mm, via-0:VIA-0.6mm, F.Cu at (205.2, 107.7)
- added REF**1111: VIA-0.6mm, via-0:VIA-0.6mm, F.Cu at (146.1, 107.7)
- added REF**1111: VIA-0.6mm, via-0:VIA-0.6mm, F.Cu at (160.8, 107.7)
- added REF**1111: VIA-0.6mm, via-0:VIA-0.6mm, F.Cu at (131.1, 107.7)
- added REF**1112: VIA-0.6mm, via-0:VIA-0.6mm, F.Cu at (175.5, 109.2)
- added REF**1112: VIA-0.6mm, via-0:VIA-0.6mm, F.Cu at (190.2, 109.2)
- added REF**1112: VIA-0.6mm, via-0:VIA-0.6mm, F.Cu at (220.0, 109.2)
- added REF**1112: VIA-0.6mm, via-0:VIA-0.6mm, F.Cu at (205.2, 109.2)
- added REF**1112: VIA-0.6mm, via-0:VIA-0.6mm, F.Cu at (146.1, 109.2)
- added REF**1112: VIA-0.6mm, via-0:VIA-0.6mm, F.Cu at (160.8, 109.2)
- added REF**1112: VIA-0.6mm, via-0:VIA-0.6mm, F.Cu at (131.1, 109.2)
- added REF**1113: VIA-0.6mm, via-0:VIA-0.6mm, F.Cu at (175.5, 110.7)
- added REF**1113: VIA-0.6mm, via-0:VIA-0.6mm, F.Cu at (190.2, 110.7)
- added REF**1113: VIA-0.6mm, via-0:VIA-0.6mm, F.Cu at (220.0, 110.7)
- added REF**1113: VIA-0.6mm, via-0:VIA-0.6mm, F.Cu at (205.2, 110.7)
- added REF**1113: VIA-0.6mm, via-0:VIA-0.6mm, F.Cu at (146.1, 110.7)
- added REF**1113: VIA-0.6mm, via-0:VIA-0.6mm, F.Cu at (160.8, 110.7)
- added REF**1113: VIA-0.6mm, via-0:VIA-0.6mm, F.Cu at (131.1, 110.7)
- added REF**1121: VIA-0.6mm, via-0:VIA-0.6mm, F.Cu at (183.6, 129.5)
- added REF**1121: VIA-0.6mm, via-0:VIA-0.6mm, F.Cu at (198.4, 129.5)
- added REF**1121: VIA-0.6mm, via-0:VIA-0.6mm, F.Cu at (228.1, 129.5)
- added REF**1121: VIA-0.6mm, via-0:VIA-0.6mm, F.Cu at (213.4, 129.5)
- added REF**1121: VIA-0.6mm, via-0:VIA-0.6mm, F.Cu at (154.2, 129.5)
- added REF**1121: VIA-0.6mm, via-0:VIA-0.6mm, F.Cu at (168.9, 129.5)
- added REF**1121: VIA-0.6mm, via-0:VIA-0.6mm, F.Cu at (139.2, 129.5)
- added REF**1122: VIA-0.6mm, via-0:VIA-0.6mm, F.Cu at (177.0, 109.2)
- added REF**1122: VIA-0.6mm, via-0:VIA-0.6mm, F.Cu at (191.7, 109.2)
- added REF**1122: VIA-0.6mm, via-0:VIA-0.6mm, F.Cu at (221.5, 109.2)
- added REF**1122: VIA-0.6mm, via-0:VIA-0.6mm, F.Cu at (206.7, 109.2)
- added REF**1122: VIA-0.6mm, via-0:VIA-0.6mm, F.Cu at (147.6, 109.2)
- added REF**1122: VIA-0.6mm, via-0:VIA-0.6mm, F.Cu at (162.3, 109.2)
- added REF**1122: VIA-0.6mm, via-0:VIA-0.6mm, F.Cu at (132.6, 109.2)
- added REF**1123: VIA-0.6mm, via-0:VIA-0.6mm, F.Cu at (177.0, 110.7)
- added REF**1123: VIA-0.6mm, via-0:VIA-0.6mm, F.Cu at (191.7, 110.7)
- added REF**1123: VIA-0.6mm, via-0:VIA-0.6mm, F.Cu at (221.5, 110.7)
- added REF**1123: VIA-0.6mm, via-0:VIA-0.6mm, F.Cu at (206.7, 110.7)
- added REF**1123: VIA-0.6mm, via-0:VIA-0.6mm, F.Cu at (147.6, 110.7)
- added REF**1123: VIA-0.6mm, via-0:VIA-0.6mm, F.Cu at (162.3, 110.7)
- added REF**1123: VIA-0.6mm, via-0:VIA-0.6mm, F.Cu at (132.6, 110.7)
- added REF**1131: VIA-0.6mm, via-0:VIA-0.6mm, F.Cu at (180.6, 110.5)
- added REF**1131: VIA-0.6mm, via-0:VIA-0.6mm, F.Cu at (195.3, 110.5)
- added REF**1131: VIA-0.6mm, via-0:VIA-0.6mm, F.Cu at (225.0, 110.5)
- added REF**1131: VIA-0.6mm, via-0:VIA-0.6mm, F.Cu at (210.3, 110.5)
- added REF**1131: VIA-0.6mm, via-0:VIA-0.6mm, F.Cu at (151.1, 110.5)
- added REF**1131: VIA-0.6mm, via-0:VIA-0.6mm, F.Cu at (165.9, 110.5)
- added REF**1131: VIA-0.6mm, via-0:VIA-0.6mm, F.Cu at (136.1, 110.5)
- added REF**1132: VIA-0.6mm, via-0:VIA-0.6mm, F.Cu at (179.1, 110.5)
- added REF**1132: VIA-0.6mm, via-0:VIA-0.6mm, F.Cu at (193.8, 110.5)
- added REF**1132: VIA-0.6mm, via-0:VIA-0.6mm, F.Cu at (223.5, 110.5)
- added REF**1132: VIA-0.6mm, via-0:VIA-0.6mm, F.Cu at (208.8, 110.5)
- added REF**1132: VIA-0.6mm, via-0:VIA-0.6mm, F.Cu at (149.6, 110.5)
- added REF**1132: VIA-0.6mm, via-0:VIA-0.6mm, F.Cu at (164.3, 110.5)
- added REF**1132: VIA-0.6mm, via-0:VIA-0.6mm, F.Cu at (134.6, 110.5)
- added REF**1133: VIA-0.6mm, via-0:VIA-0.6mm, F.Cu at (180.6, 108.0)
- added REF**1133: VIA-0.6mm, via-0:VIA-0.6mm, F.Cu at (195.3, 108.0)
- added REF**1133: VIA-0.6mm, via-0:VIA-0.6mm, F.Cu at (225.0, 108.0)
- added REF**1133: VIA-0.6mm, via-0:VIA-0.6mm, F.Cu at (210.3, 108.0)
- added REF**1133: VIA-0.6mm, via-0:VIA-0.6mm, F.Cu at (151.1, 108.0)
- added REF**1133: VIA-0.6mm, via-0:VIA-0.6mm, F.Cu at (165.9, 108.0)
- added REF**1133: VIA-0.6mm, via-0:VIA-0.6mm, F.Cu at (136.1, 108.0)
- added REF**1141: VIA-0.6mm, via-0:VIA-0.6mm, F.Cu at (177.8, 108.0)
- added REF**1141: VIA-0.6mm, via-0:VIA-0.6mm, F.Cu at (192.5, 108.0)
- added REF**1141: VIA-0.6mm, via-0:VIA-0.6mm, F.Cu at (222.2, 108.0)
- added REF**1141: VIA-0.6mm, via-0:VIA-0.6mm, F.Cu at (207.5, 108.0)
- added REF**1141: VIA-0.6mm, via-0:VIA-0.6mm, F.Cu at (148.3, 108.0)
- added REF**1141: VIA-0.6mm, via-0:VIA-0.6mm, F.Cu at (163.1, 108.0)
- added REF**1141: VIA-0.6mm, via-0:VIA-0.6mm, F.Cu at (133.3, 108.0)
- added REF**1142: VIA-0.6mm, via-0:VIA-0.6mm, F.Cu at (177.8, 110.5)
- added REF**1142: VIA-0.6mm, via-0:VIA-0.6mm, F.Cu at (192.5, 110.5)
- added REF**1142: VIA-0.6mm, via-0:VIA-0.6mm, F.Cu at (222.2, 110.5)
- added REF**1142: VIA-0.6mm, via-0:VIA-0.6mm, F.Cu at (207.5, 110.5)
- added REF**1142: VIA-0.6mm, via-0:VIA-0.6mm, F.Cu at (148.3, 110.5)
- added REF**1142: VIA-0.6mm, via-0:VIA-0.6mm, F.Cu at (163.1, 110.5)
- added REF**1142: VIA-0.6mm, via-0:VIA-0.6mm, F.Cu at (133.3, 110.5)
- added REF**1143: VIA-0.6mm, via-0:VIA-0.6mm, F.Cu at (178.6, 109.2)
- added REF**1143: VIA-0.6mm, via-0:VIA-0.6mm, F.Cu at (193.3, 109.2)
- added REF**1143: VIA-0.6mm, via-0:VIA-0.6mm, F.Cu at (223.0, 109.2)
- added REF**1143: VIA-0.6mm, via-0:VIA-0.6mm, F.Cu at (208.3, 109.2)
- added REF**1143: VIA-0.6mm, via-0:VIA-0.6mm, F.Cu at (149.1, 109.2)
- added REF**1143: VIA-0.6mm, via-0:VIA-0.6mm, F.Cu at (163.8, 109.2)
- added REF**1143: VIA-0.6mm, via-0:VIA-0.6mm, F.Cu at (134.1, 109.2)
- added REF**1151: VIA-0.6mm, via-0:VIA-0.6mm, F.Cu at (176.8, 108.0)
- added REF**1151: VIA-0.6mm, via-0:VIA-0.6mm, F.Cu at (191.5, 108.0)
- added REF**1151: VIA-0.6mm, via-0:VIA-0.6mm, F.Cu at (221.2, 108.0)
- added REF**1151: VIA-0.6mm, via-0:VIA-0.6mm, F.Cu at (206.5, 108.0)
- added REF**1151: VIA-0.6mm, via-0:VIA-0.6mm, F.Cu at (147.3, 108.0)
- added REF**1151: VIA-0.6mm, via-0:VIA-0.6mm, F.Cu at (162.1, 108.0)
- added REF**1151: VIA-0.6mm, via-0:VIA-0.6mm, F.Cu at (132.3, 108.0)
- added REF**1152: VIA-0.6mm, via-0:VIA-0.6mm, F.Cu at (179.1, 108.0)
- added REF**1152: VIA-0.6mm, via-0:VIA-0.6mm, F.Cu at (193.8, 108.0)
- added REF**1152: VIA-0.6mm, via-0:VIA-0.6mm, F.Cu at (223.5, 108.0)
- added REF**1152: VIA-0.6mm, via-0:VIA-0.6mm, F.Cu at (208.8, 108.0)
- added REF**1152: VIA-0.6mm, via-0:VIA-0.6mm, F.Cu at (149.6, 108.0)
- added REF**1152: VIA-0.6mm, via-0:VIA-0.6mm, F.Cu at (164.3, 108.0)
- added REF**1152: VIA-0.6mm, via-0:VIA-0.6mm, F.Cu at (134.6, 108.0)
- added REF**1153: VIA-0.6mm, via-0:VIA-0.6mm, F.Cu at (184.7, 130.8)
- added REF**1153: VIA-0.6mm, via-0:VIA-0.6mm, F.Cu at (197.1, 120.4)
- added REF**1153: VIA-0.6mm, via-0:VIA-0.6mm, F.Cu at (198.9, 130.3)
- added REF**1153: VIA-0.6mm, via-0:VIA-0.6mm, F.Cu at (198.6, 120.7)
- added REF**1153: VIA-0.6mm, via-0:VIA-0.6mm, F.Cu at (196.3, 119.6)
- added REF**1153: VIA-0.6mm, via-0:VIA-0.6mm, F.Cu at (199.4, 125.0)
- added REF**1153: VIA-0.6mm, via-0:VIA-0.6mm, F.Cu at (191.5, 110.5)
- added REF**1153: VIA-0.6mm, via-0:VIA-0.6mm, F.Cu at (195.8, 118.6)
- added REF**1153: VIA-0.6mm, via-0:VIA-0.6mm, F.Cu at (196.5, 112.5)
- added REF**1153: VIA-0.6mm, via-0:VIA-0.6mm, F.Cu at (199.4, 130.8)
- added REF**1153: VIA-0.6mm, via-0:VIA-0.6mm, F.Cu at (229.1, 130.8)
- added REF**1153: VIA-0.6mm, via-0:VIA-0.6mm, F.Cu at (181.8, 112.5)
- added REF**1153: VIA-0.6mm, via-0:VIA-0.6mm, F.Cu at (226.2, 112.5)
- added REF**1153: VIA-0.6mm, via-0:VIA-0.6mm, F.Cu at (225.6, 118.6)
- added REF**1153: VIA-0.6mm, via-0:VIA-0.6mm, F.Cu at (221.2, 110.5)
- added REF**1153: VIA-0.6mm, via-0:VIA-0.6mm, F.Cu at (229.1, 125.0)
- added REF**1153: VIA-0.6mm, via-0:VIA-0.6mm, F.Cu at (226.1, 119.6)
- added REF**1153: VIA-0.6mm, via-0:VIA-0.6mm, F.Cu at (228.3, 120.7)
- added REF**1153: VIA-0.6mm, via-0:VIA-0.6mm, F.Cu at (228.6, 130.3)
- added REF**1153: VIA-0.6mm, via-0:VIA-0.6mm, F.Cu at (226.8, 120.4)
- added REF**1153: VIA-0.6mm, via-0:VIA-0.6mm, F.Cu at (212.1, 120.4)
- added REF**1153: VIA-0.6mm, via-0:VIA-0.6mm, F.Cu at (213.9, 130.3)
- added REF**1153: VIA-0.6mm, via-0:VIA-0.6mm, F.Cu at (181.1, 118.6)
- added REF**1153: VIA-0.6mm, via-0:VIA-0.6mm, F.Cu at (213.6, 120.7)
- added REF**1153: VIA-0.6mm, via-0:VIA-0.6mm, F.Cu at (211.3, 119.6)
- added REF**1153: VIA-0.6mm, via-0:VIA-0.6mm, F.Cu at (214.4, 125.0)
- added REF**1153: VIA-0.6mm, via-0:VIA-0.6mm, F.Cu at (206.5, 110.5)
- added REF**1153: VIA-0.6mm, via-0:VIA-0.6mm, F.Cu at (210.8, 118.6)
- added REF**1153: VIA-0.6mm, via-0:VIA-0.6mm, F.Cu at (211.5, 112.5)
- added REF**1153: VIA-0.6mm, via-0:VIA-0.6mm, F.Cu at (214.4, 130.8)
- added REF**1153: VIA-0.6mm, via-0:VIA-0.6mm, F.Cu at (155.2, 130.8)
- added REF**1153: VIA-0.6mm, via-0:VIA-0.6mm, F.Cu at (152.3, 112.5)
- added REF**1153: VIA-0.6mm, via-0:VIA-0.6mm, F.Cu at (151.6, 118.6)
- added REF**1153: VIA-0.6mm, via-0:VIA-0.6mm, F.Cu at (176.8, 110.5)
- added REF**1153: VIA-0.6mm, via-0:VIA-0.6mm, F.Cu at (147.3, 110.5)
- added REF**1153: VIA-0.6mm, via-0:VIA-0.6mm, F.Cu at (155.2, 125.0)
- added REF**1153: VIA-0.6mm, via-0:VIA-0.6mm, F.Cu at (152.1, 119.6)
- added REF**1153: VIA-0.6mm, via-0:VIA-0.6mm, F.Cu at (154.4, 120.7)
- added REF**1153: VIA-0.6mm, via-0:VIA-0.6mm, F.Cu at (154.7, 130.3)
- added REF**1153: VIA-0.6mm, via-0:VIA-0.6mm, F.Cu at (152.9, 120.4)
- added REF**1153: VIA-0.6mm, via-0:VIA-0.6mm, F.Cu at (167.6, 120.4)
- added REF**1153: VIA-0.6mm, via-0:VIA-0.6mm, F.Cu at (169.4, 130.3)
- added REF**1153: VIA-0.6mm, via-0:VIA-0.6mm, F.Cu at (169.2, 120.7)
- added REF**1153: VIA-0.6mm, via-0:VIA-0.6mm, F.Cu at (166.9, 119.6)
- added REF**1153: VIA-0.6mm, via-0:VIA-0.6mm, F.Cu at (184.7, 125.0)
- added REF**1153: VIA-0.6mm, via-0:VIA-0.6mm, F.Cu at (169.9, 125.0)
- added REF**1153: VIA-0.6mm, via-0:VIA-0.6mm, F.Cu at (162.1, 110.5)
- added REF**1153: VIA-0.6mm, via-0:VIA-0.6mm, F.Cu at (166.4, 118.6)
- added REF**1153: VIA-0.6mm, via-0:VIA-0.6mm, F.Cu at (167.0, 112.5)
- added REF**1153: VIA-0.6mm, via-0:VIA-0.6mm, F.Cu at (169.9, 130.8)
- added REF**1153: VIA-0.6mm, via-0:VIA-0.6mm, F.Cu at (140.2, 130.8)
- added REF**1153: VIA-0.6mm, via-0:VIA-0.6mm, F.Cu at (137.3, 112.5)
- added REF**1153: VIA-0.6mm, via-0:VIA-0.6mm, F.Cu at (136.7, 118.6)
- added REF**1153: VIA-0.6mm, via-0:VIA-0.6mm, F.Cu at (132.3, 110.5)
- added REF**1153: VIA-0.6mm, via-0:VIA-0.6mm, F.Cu at (140.2, 125.0)
- added REF**1153: VIA-0.6mm, via-0:VIA-0.6mm, F.Cu at (181.6, 119.6)
- added REF**1153: VIA-0.6mm, via-0:VIA-0.6mm, F.Cu at (137.2, 119.6)
- added REF**1153: VIA-0.6mm, via-0:VIA-0.6mm, F.Cu at (139.4, 120.7)
- added REF**1153: VIA-0.6mm, via-0:VIA-0.6mm, F.Cu at (139.7, 130.3)
- added REF**1153: VIA-0.6mm, via-0:VIA-0.6mm, F.Cu at (137.9, 120.4)
- added REF**1153: VIA-0.6mm, via-0:VIA-0.6mm, F.Cu at (183.9, 120.7)
- added REF**1153: VIA-0.6mm, via-0:VIA-0.6mm, F.Cu at (184.2, 130.3)
- added REF**1153: VIA-0.6mm, via-0:VIA-0.6mm, F.Cu at (182.4, 120.4)
- added U11: 24C16, SMD_Packages:SOIC-8-N, F.Cu at (178.6, 109.2)
- added U11: 24C16, SMD_Packages:SOIC-8-N, F.Cu at (193.3, 109.2)
- added U11: 24C16, SMD_Packages:SOIC-8-N, F.Cu at (223.0, 109.2)
- added U11: 24C16, SMD_Packages:SOIC-8-N, F.Cu at (208.3, 109.2)
- added U11: 24C16, SMD_Packages:SOIC-8-N, F.Cu at (149.1, 109.2)
- added U11: 24C16, SMD_Packages:SOIC-8-N, F.Cu at (163.8, 109.2)
- added U11: 24C16, SMD_Packages:SOIC-8-N, F.Cu at (134.1, 109.2)
- added U2: MAX31820, TO_SOT_Packages_THT:TO-92_Molded_Wide, F.Cu at (184.2, 122.7)
- added U2: MAX31820, TO_SOT_Packages_THT:TO-92_Molded_Wide, F.Cu at (198.9, 122.7)
- added U2: MAX31820, TO_SOT_Packages_THT:TO-92_Molded_Wide, F.Cu at (228.6, 122.7)
- added U2: MAX31820, TO_SOT_Packages_THT:TO-92_Molded_Wide, F.Cu at (213.9, 122.7)
- added U2: MAX31820, TO_SOT_Packages_THT:TO-92_Molded_Wide, F.Cu at (154.7, 122.7)
- added U2: MAX31820, TO_SOT_Packages_THT:TO-92_Molded_Wide, F.Cu at (169.4, 122.7)
- added U2: MAX31820, TO_SOT_Packages_THT:TO-92_Molded_Wide, F.Cu at (139.7, 122.7)
- moved REF**1153 31.2 mm to (125.5, 130.8)
- moved REF**1153 30.7 mm to (117.6, 110.5)
- moved REF**1121 30.3 mm to (124.5, 129.5)
- moved REF**1151 29.5 mm to (117.6, 108.0)
- moved P2 28.7 mm to (124.5, 118.4), turned to 180 degrees
- moved REF**1153 27.3 mm to (123.2, 120.4)
- moved REF**1142 27.1 mm to (118.6, 110.5)
- moved REF**1152 27.1 mm to (119.9, 108.0)
- moved REF**1141 27.0 mm to (118.6, 108.0)
- moved REF**1143 26.1 mm to (119.4, 109.2)
- moved REF**1153 26.1 mm to (122.4, 119.6)
- moved REF**1153 25.4 mm to (124.7, 120.7)
- moved REF**1153 25.2 mm to (125.5, 125.0)
- moved REF**1153 25.1 mm to (125.0, 130.3)
- moved REF**1153 24.9 mm to (121.9, 118.6)
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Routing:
- net TX: track 14.8 -> 211.4 mm
- net VCC: track 26.3 -> 210.1 mm
- net RX: track 14.3 -> 141.3 mm
- net DATA: track 15.9 -> 127.5 mm
- net SCL: track 4.92 -> 39.3 mm
- net GND: track 4.87 -> 39.0 mm
- net Net-(P1-Pad10): track 4.22 -> 33.8 mm
- net SDA: track 3.39 -> 27.2 mm
- net Net-(D1-Pad2): track 2.59 -> 20.7 mm
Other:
- board size 27.9 x 27.9 mm -> 117.6 x 28.4 mm
- board text added: "IoTAD v1.2.1 15/03/2016 JGV"
- board text removed: "IoTAD v1.2 24/02/2016 JGV"
